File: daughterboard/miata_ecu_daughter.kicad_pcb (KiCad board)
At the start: 4 copper layers, 125 x 60 mm, 232 parts, among them J1 Mezz_Power_Out, J102 SWD (WBO), J2 Mezz_Signal_In, J3 SWD, Q1 AUIPS2041LTR, Q101 VND14NV04, Q2 AUIPS2041LTR, Q3 AUIPS2041LTR, Q4 AUIPS2041LTR, Q5 AUIPS2041LTR, Q6 AUIPS2041LTR, Q7 AUIPS2041LTR, Q8 AUIPS2041LTR, SW1 BOOT, SW2 RESET, U1 STM32F407VGT6, U10 SN65HVD230DR, U101 MCP6004, U102 STM32F042K6T6, U103 REF3033, U105 AD8628, U106 SN65HVD230DR, U11 SN74LVC4245APWR, U2 LMR14020, U3 TLS115B0EJ, U4 AMS1117-3.3, U5 ULN2003AD, U6 TC4427, U7 TC4427, U8 LMV321IDBVR, U9 MAX9926UAEE+, Y1 8MHz

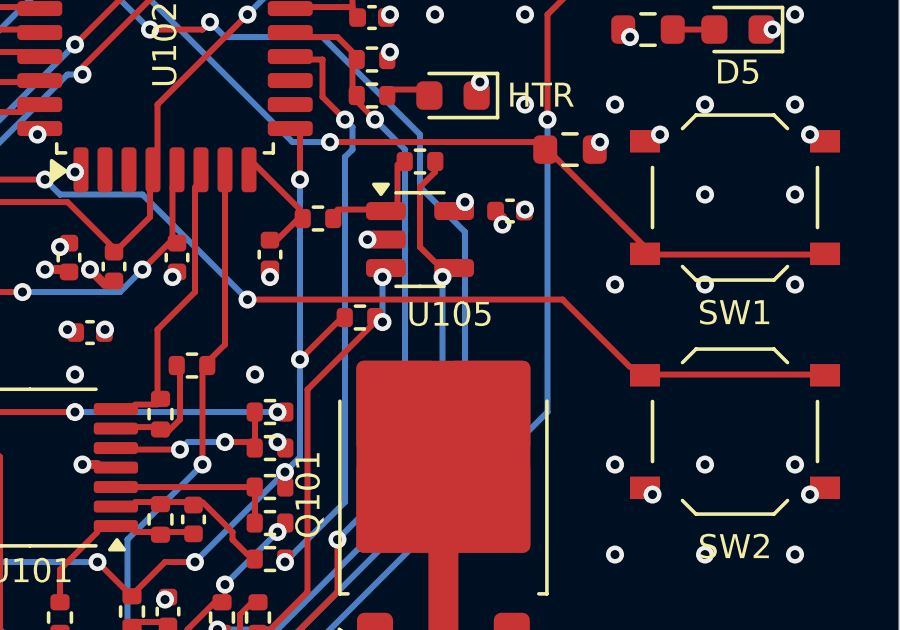
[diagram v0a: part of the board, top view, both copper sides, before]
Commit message: Daughterboard rev 0.5b: in-stock parts for JLCPCB assembly
JLCPCB's BOM check flagged ten lines short of stock and one footprint mismatch.
All replacements are in stock at JLCPCB and fit the existing footprints (no re-route):
- Q1-Q8: onsemi NCV8406ASTT3G (C459816) instead of AUIPS2041LTR: same SOT-223
  pinout, 60-70 V active clamp, current limit, thermal shutdown, AEC-Q101.
- D11/D12 Littelfuse SMAJ33A (C223988); F1 TECHFUSE nSMD050-33V (C70077);
  L1 FH CMI322513U2R2KT (C70960); LEDs KENTO KT-0603G/B/Y; C103 YAGEO 33 nF
  50 V (C106862); R110 62 ohm 1% (C23222, was 61.9).
- U9 (MAX9926, spare VR inputs, out of stock everywhere) not fitted.
- U105 footprint renamed SOT-23-5 (AD8628ARTZ; pads identical to TSOT-23-5).
- JLC BOM: one line per LCSC part (SW1/SW2); not-fitted parts excluded.

Re-checked: netlist 754 pads 0 differences, DRC 0 unconnected / 0 clearance,
circuit sims with the NCV8406A model 20 OK / 3 CHECK / 6 REF / 0 FAIL.

Co-Authored-By: Claude Opus 5.5 <noreply@anthropic.com>
Claude-Session: https://claude.ai/code/session_012UFcA8PhPqkqYxcgEjD2n9
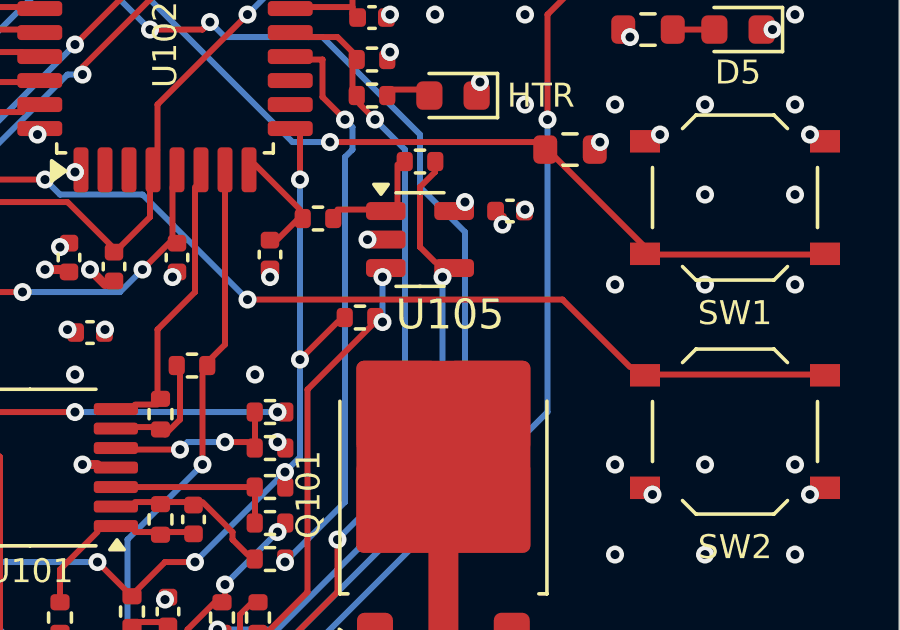
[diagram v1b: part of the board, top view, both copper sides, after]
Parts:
- F1: value SMD1206P050TF/24 -> nSMD050-33V
- Q1, Q2, Q3, Q4, Q5, Q6, Q7, Q8: value AUIPS2041LTR -> NCV8406ASTT3G
- R110: value 61.9 -> 62
- U105: footprint Package_TO_SOT_SMD:TSOT-23-5 -> Package_TO_SOT_SMD:SOT-23-5
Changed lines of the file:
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@@
         (effects (font (size 0.8 0.8) (thickness 0.12)))
     )
-    (fp_text value "AUIPS2041LTR" (at 0 4.5 90) (layer "F.Fab") hide
+    (fp_text value "NCV8406ASTT3G" (at 0 4.5 90) (layer "F.Fab") hide
         (effects (font (size 1 1) (thickness 0.15)))
     )
@@
     )
   )
+  (footprint "Package_TO_SOT_SMD:SOT-23-5" (layer "F.Cu")
+    (at 209 89)
+    (descr "SOT, 5 Pin (https://www.jedec.org/sites/default/files/docs/Mo-178c.PDF variant AA), generated with kicad-footprint-generator ipc_gullwing_generator.py")
+    (tags "SOT TO_SOT_SMD")
+    (attr smd)
+    (fp_text reference "U105" (at 1 2.5) (layer "F.SilkS")
+        (effects (font (size 1 1) (thickness 0.15)))
+    )
+    (fp_text value "AD8628" (at 0 2.4) (layer "F.Fab") hide
+        (effects (font (size 1 1) (thickness 0.15)))
+    )
+    (fp_text user "${REFERENCE}" (at 0 0) (layer "F.Fab")
+        (effects (font (size 0.4 0.4) (thickness 0.06)))
+    )
+    (fp_line (start 0 -1.56) (end -0.8 -1.56)
+      (stroke (width 0.12) (type solid)) (layer "F.SilkS"))
+    (fp_line (start 0 -1.56) (end 0.8 -1.56)
+      (stroke (width 0.12) (type solid)) (layer "F.SilkS"))
+    (fp_line (start 0 1.56) (end -0.8 1.56)
+      (stroke (width 0.12) (type solid)) (layer "F.SilkS"))
+    (fp_line (start 0 1.56) (end 0.8 1.56)
+      (stroke (width 0.12) (type solid)) (layer "F.SilkS"))
+    (fp_poly
+      (pts
+        (xy -1.3 -1.51)
+        (xy -1.54 -1.84)
+        (xy -1.06 -1.84)
+        (xy -1.3 -1.51)
+      )
+      (stroke (width 0.12) (type solid)) (fill solid) (layer "F.SilkS"))
+    (fp_line (start -2.05 -1.7) (end -2.05 1.7)
+      (stroke (width 0.05) (type solid)) (layer "F.CrtYd"))
+    (fp_line (start -2.05 1.7) (end 2.05 1.7)
+      (stroke (width 0.05) (type solid)) (layer "F.CrtYd"))
+    (fp_line (start 2.05 -1.7) (end -2.05 -1.7)
+      (stroke (width 0.05) (type solid)) (layer "F.CrtYd"))
+    (fp_line (start 2.05 1.7) (end 2.05 -1.7)
+      (stroke (width 0.05) (type solid)) (layer "F.CrtYd"))
+    (fp_line (start -0.8 -1.05) (end -0.4 -1.45)
+      (stroke (width 0.1) (type solid)) (layer "F.Fab"))
+    (fp_line (start -0.8 1.45) (end -0.8 -1.05)
+      (stroke (width 0.1) (type solid)) (layer "F.Fab"))
+    (fp_line (start -0.4 -1.45) (end 0.8 -1.45)
+      (stroke (width 0.1) (type solid)) (layer "F.Fab"))
+    (fp_line (start 0.8 -1.45) (end 0.8 1.45)
+      (stroke (width 0.1) (type solid)) (layer "F.Fab"))
+    (fp_line (start 0.8 1.45) (end -0.8 1.45)
+      (stroke (width 0.1) (type solid)) (layer "F.Fab"))
+    (pad "1" smd roundrect (at -1.1375 -0.95) (size 1.325 0.6) (layers "F.Cu" "F.Paste" "F.Mask") (roundrect_rratio 0.25)
+      (net 162 "/Wideband controller/WB_IS_OUT"))
+    (pad "2" smd roundrect (at -1.1375 0) (size 1.325 0.6) (layers "F.Cu" "F.Paste" "F.Mask") (roundrect_rratio 0.25)
+      (net 39 "GND"))
+    (pad "3" smd roundrect (at -1.1375 0.95) (size 1.325 0.6) (layers "F.Cu" "F.Paste" "F.Mask") (roundrect_rratio 0.25)
+      (net 163 "/Wideband controller/WB_IS_P"))
+    (pad "4" smd roundrect (at 1.1375 0.95) (size 1.325 0.6) (layers "F.Cu" "F.Paste" "F.Mask") (roundrect_rratio 0.25)
+      (net 161 "/Wideband controller/WB_IS_N"))
+    (pad "5" smd roundrect (at 1.1375 -0.95) (size 1.325 0.6) (layers "F.Cu" "F.Paste" "F.Mask") (roundrect_rratio 0.25)
+      (net 4 "+3V3"))
+    (model "${KICAD7_3DMODEL_DIR}/Package_TO_SOT_SMD.3dshapes/SOT-23-5.wrl"
+      (offset (xyz 0 0 0))
+      (scale (xyz 1 1 1))
+      (rotate (xyz 0 0 0))
+    )
+  )
   (footprint "Resistor_SMD:R_0603_1608Metric" (layer "F.Cu")
     (at 115.6 92.6)
@@
         (effects (font (size 0.8 0.8) (thickness 0.12)))
     )
-    (fp_text value "AUIPS2041LTR" (at 0 4.5 90) (layer "F.Fab") hide
+    (fp_text value "NCV8406ASTT3G" (at 0 4.5 90) (layer "F.Fab") hide
         (effects (font (size 1 1) (thickness 0.15)))
     )
@@
         (effects (font (size 0.8 0.8) (thickness 0.12)))
     )
-    (fp_text value "61.9" (at 0 1.43) (layer "F.Fab") hide
+    (fp_text value "62" (at 0 1.43) (layer "F.Fab") hide
         (effects (font (size 1 1) (thickness 0.15)))
     )
@@
         (effects (font (size 0.8 0.8) (thickness 0.12)))
     )
-    (fp_text value "AUIPS2041LTR" (at 0 4.5 90) (layer "F.Fab") hide
+    (fp_text value "NCV8406ASTT3G" (at 0 4.5 90) (layer "F.Fab") hide
         (effects (font (size 1 1) (thickness 0.15)))
     )
@@
         (effects (font (size 0.8 0.8) (thickness 0.12)))
     )
-    (fp_text value "AUIPS2041LTR" (at 0 4.5 90) (layer "F.Fab") hide
+    (fp_text value "NCV8406ASTT3G" (at 0 4.5 90) (layer "F.Fab") hide
         (effects (font (size 1 1) (thickness 0.15)))
     )
@@
         (effects (font (size 0.8 0.8) (thickness 0.12)))
     )
-    (fp_text value "AUIPS2041LTR" (at 0 4.5 90) (layer "F.Fab") hide
+    (fp_text value "NCV8406ASTT3G" (at 0 4.5 90) (layer "F.Fab") hide
         (effects (font (size 1 1) (thickness 0.15)))
     )
@@
         (effects (font (size 0.8 0.8) (thickness 0.12)))
     )
-    (fp_text value "AUIPS2041LTR" (at 0 4.5 90) (layer "F.Fab") hide
+    (fp_text value "NCV8406ASTT3G" (at 0 4.5 90) (layer "F.Fab") hide
         (effects (font (size 1 1) (thickness 0.15)))
     )
@@
         (effects (font (size 0.8 0.8) (thickness 0.12)))
     )
-    (fp_text value "AUIPS2041LTR" (at 0 4.5 90) (layer "F.Fab") hide
+    (fp_text value "NCV8406ASTT3G" (at 0 4.5 90) (layer "F.Fab") hide
         (effects (font (size 1 1) (thickness 0.15)))
     )
@@
         (effects (font (size 0.8 0.8) (thickness 0.12)))
     )
-    (fp_text value "SMD1206P050TF/24" (at 0 1.82) (layer "F.Fab") hide
+    (fp_text value "nSMD050-33V" (at 0 1.82) (layer "F.Fab") hide
         (effects (font (size 1 1) (thickness 0.15)))
     )
@@
     )
   )
-  (footprint "Package_TO_SOT_SMD:TSOT-23-5" (layer "F.Cu")
-    (at 209 89)
-    (descr "TSOT, 5 Pin (https://www.jedec.org/sites/default/files/docs/MO-193D.pdf variant AB), generated with kicad-footprint-generator ipc_gullwing_generator.py")
-    (tags "TSOT TO_SOT_SMD")
-    (property "LCSC" "C29309")
-    (attr smd)
-    (fp_text reference "U105" (at 1 2.5) (layer "F.SilkS")
-        (effects (font (size 0.8 0.8) (thickness 0.12)))
-    )
-    (fp_text value "AD8628" (at 0 2.4) (layer "F.Fab") hide
-        (effects (font (size 1 1) (thickness 0.15)))
-    )
-    (fp_text user "${REFERENCE}" (at 0 0) (layer "F.Fab")
-        (effects (font (size 0.4 0.4) (thickness 0.06)))
-    )
-    (fp_line (start 0 -1.56) (end -0.8 -1.56)
-      (stroke (width 0.12) (type solid)) (layer "F.SilkS"))
-    (fp_line (start 0 -1.56) (end 0.8 -1.56)
-      (stroke (width 0.12) (type solid)) (layer "F.SilkS"))
-    (fp_line (start 0 1.56) (end -0.8 1.56)
-      (stroke (width 0.12) (type solid)) (layer "F.SilkS"))
-    (fp_line (start 0 1.56) (end 0.8 1.56)
-      (stroke (width 0.12) (type solid)) (layer "F.SilkS"))
-    (fp_poly
-      (pts
-        (xy -1.3 -1.51)
-        (xy -1.54 -1.84)
-        (xy -1.06 -1.84)
-        (xy -1.3 -1.51)
-      )
-      (stroke (width 0.12) (type solid)) (fill solid) (layer "F.SilkS"))
-    (fp_line (start -2.05 -1.7) (end -2.05 1.7)
-      (stroke (width 0.05) (type solid)) (layer "F.CrtYd"))
-    (fp_line (start -2.05 1.7) (end 2.05 1.7)
-      (stroke (width 0.05) (type solid)) (layer "F.CrtYd"))
-    (fp_line (start 2.05 -1.7) (end -2.05 -1.7)
-      (stroke (width 0.05) (type solid)) (layer "F.CrtYd"))
-    (fp_line (start 2.05 1.7) (end 2.05 -1.7)
-      (stroke (width 0.05) (type solid)) (layer "F.CrtYd"))
-    (fp_line (start -0.8 -1.05) (end -0.4 -1.45)
-      (stroke (width 0.1) (type solid)) (layer "F.Fab"))
-    (fp_line (start -0.8 1.45) (end -0.8 -1.05)
-      (stroke (width 0.1) (type solid)) (layer "F.Fab"))
-    (fp_line (start -0.4 -1.45) (end 0.8 -1.45)
-      (stroke (width 0.1) (type solid)) (layer "F.Fab"))
-    (fp_line (start 0.8 -1.45) (end 0.8 1.45)
-      (stroke (width 0.1) (type solid)) (layer "F.Fab"))
-    (fp_line (start 0.8 1.45) (end -0.8 1.45)
-      (stroke (width 0.1) (type solid)) (layer "F.Fab"))
-    (pad "1" smd roundrect (at -1.1375 -0.95) (size 1.325 0.6) (layers "F.Cu" "F.Paste" "F.Mask") (roundrect_rratio 0.25)
-      (net 162 "/Wideband controller/WB_IS_OUT"))
-    (pad "2" smd roundrect (at -1.1375 0) (size 1.325 0.6) (layers "F.Cu" "F.Paste" "F.Mask") (roundrect_rratio 0.25)
-      (net 39 "GND"))
-    (pad "3" smd roundrect (at -1.1375 0.95) (size 1.325 0.6) (layers "F.Cu" "F.Paste" "F.Mask") (roundrect_rratio 0.25)
-      (net 163 "/Wideband controller/WB_IS_P"))
-    (pad "4" smd roundrect (at 1.1375 0.95) (size 1.325 0.6) (layers "F.Cu" "F.Paste" "F.Mask") (roundrect_rratio 0.25)
-      (net 161 "/Wideband controller/WB_IS_N"))
-    (pad "5" smd roundrect (at 1.1375 -0.95) (size 1.325 0.6) (layers "F.Cu" "F.Paste" "F.Mask") (roundrect_rratio 0.25)
-      (net 4 "+3V3"))
-    (model "${KICAD7_3DMODEL_DIR}/Package_TO_SOT_SMD.3dshapes/TSOT-23-5.wrl"
-      (offset (xyz 0 0 0))
-      (scale (xyz 1 1 1))
-      (rotate (xyz 0 0 0))
-    )
-  )
   (footprint "Capacitor_SMD:C_0603_1608Metric" (layer "F.Cu")
     (at 153.2 72)
@@
         (effects (font (size 0.8 0.8) (thickness 0.12)))
     )
-    (fp_text value "AUIPS2041LTR" (at 0 4.5 90) (layer "F.Fab") hide
+    (fp_text value "NCV8406ASTT3G" (at 0 4.5 90) (layer "F.Fab") hide
         (effects (font (size 1 1) (thickness 0.15)))
     )

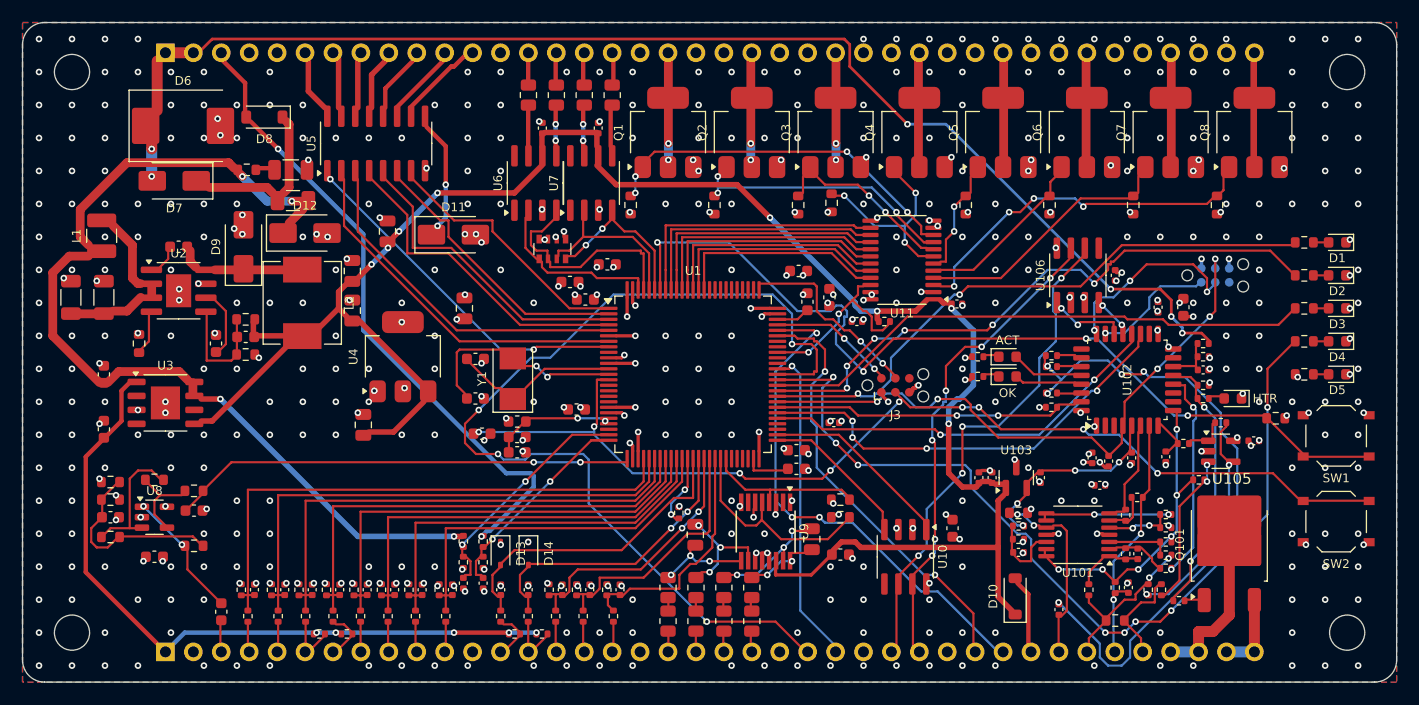
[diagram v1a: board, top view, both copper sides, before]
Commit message: Daughterboard rev 0.5b: LM2903 VR conditioner, JLC placement fix, parts-availability swaps
- U9: the out-of-stock, single-source MAX9926 is replaced by an LM2903 dual comparator (TI, onsemi, UMW, ST...).
  Each VR input gets a BAT54S clamp to GND/+5V and 100k to a 1.65 V bias, each output 1M of hysteresis
  (D15-D18, R73-R80, C60). Same output polarity, so J2 wiring and firmware are unchanged. circuit_sim.py
  section H covers it (25 OK / 4 CHECK / 6 REF / 0 FAIL).
- Re-routed; daughter_patch_05b.py (with hand_route.py) routes HALL1, which the autorouter left open, and
  moves AN_AUX3 clear of the new clamps. Netlist 778 pads, 0 differences; DRC 0 unconnected, 0 clearance.
- CPLs for all boards now use the gerbers' own coordinates, with JLC's per-package rotation offsets
  (SOT-223/TO-252/SOT-23 +180, SOIC/TSSOP/LQFP +270, resistor arrays +90).
- Parts-availability review swaps: motherboard F4 to TECHFUSE nSMD050-33V (C70077; the old PTC is out of
  stock), D6 to Littelfuse SMCJ30A, D9 to Diodes B360A. MPX5700AP (NRND), the harness headers and the
  STM32F042 are recorded as supply open items in VERIFICATION.md.
- Viewer assets and README renders rebuilt.

Co-Authored-By: Claude Opus 5.5 <noreply@anthropic.com>
Claude-Session: https://claude.ai/code/session_012UFcA8PhPqkqYxcgEjD2n9
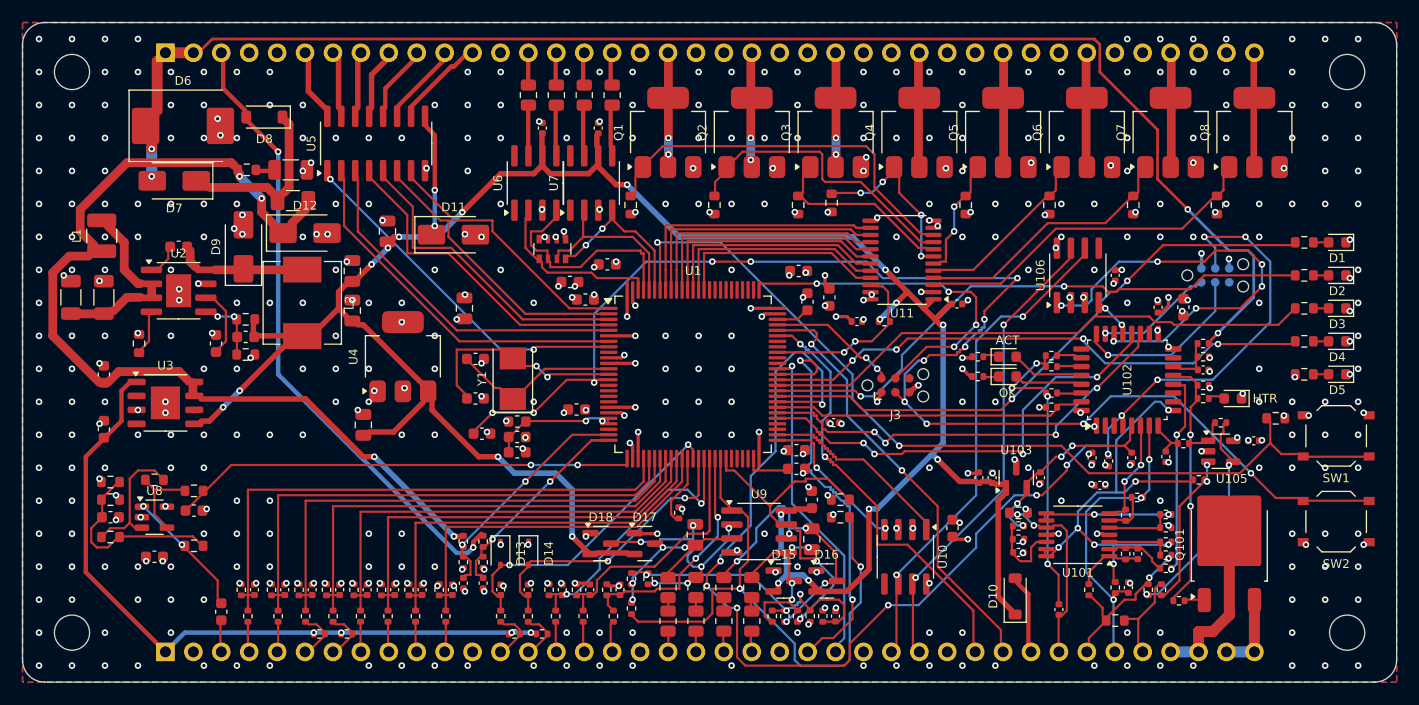
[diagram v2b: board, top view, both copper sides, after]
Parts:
- added C60: 100n, Capacitor_SMD:C_0402_1005Metric, F.Cu at (173.9, 104.0)
- added D15: BAT54S, Package_TO_SOT_SMD:SOT-23, F.Cu at (169.2, 100.8)
- added D16: BAT54S, Package_TO_SOT_SMD:SOT-23, F.Cu at (173.2, 100.8)
- added D17: BAT54S, Package_TO_SOT_SMD:SOT-23, F.Cu at (156.6, 97.4)
- added D18: BAT54S, Package_TO_SOT_SMD:SOT-23, F.Cu at (152.6, 97.4)
- added R73: 100k, Resistor_SMD:R_0402_1005Metric, F.Cu at (168.2, 104.0)
- added R74: 100k, Resistor_SMD:R_0402_1005Metric, F.Cu at (169.3, 104.0)
- added R75: 100k, Resistor_SMD:R_0402_1005Metric, F.Cu at (155.4, 100.6)
- added R76: 100k, Resistor_SMD:R_0402_1005Metric, F.Cu at (156.9, 100.6)
- added R77: 1M, Resistor_SMD:R_0402_1005Metric, F.Cu at (170.5, 104.0)
- added R78: 1M, Resistor_SMD:R_0402_1005Metric, F.Cu at (155.4, 103.3)
- added R79: 10k, Resistor_SMD:R_0402_1005Metric, F.Cu at (171.7, 104.0)
- added R80: 10k, Resistor_SMD:R_0402_1005Metric, F.Cu at (172.8, 104.0)
- D9: value SS36 -> B360A
- U9: value MAX9926UAEE+ -> LM2903DR; footprint Package_SO:QSOP-16_3.9x4.9mm_P0.635mm -> Package_SO:SOIC-8_3.9x4.9mm_P1.27mm
- moved C50 5.64 mm to (171.8, 93.4), turned to 90 degrees
- moved U9 0.60 mm to (167.0, 96.3), turned to 0 degrees
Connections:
- U9 pad 1: GND -> VR2_OUT
- U9 pad 2: (no net) -> /Inputs/VR2_INN
- U9 pad 3: GND -> /Inputs/VR2_INP
- U9 pad 4: VR1_OUT -> GND
- U9 pad 5: VR2_OUT -> /Inputs/VR1_INP
- U9 pad 6: GND -> /Inputs/VR1_INN
- U9 pad 7: (no net) -> VR1_OUT
- U9 pad 8: GND -> +5V
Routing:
- net WB_NRST: track 54.3 -> 123.9 mm, vias 5 -> 12
- net UART_TX: track 89.0 -> 37.2 mm, vias 4 -> 2
- net +5V: track 153.5 -> 192.2 mm, vias 8 -> 18
- net VR2_OUT: track 18.8 -> 52.4 mm, vias 0 -> 2
- net /Wideband controller/WB_CAN_TX: track 6.22 -> 39.3 mm, vias 2 -> 6
- net /MCU/NRST: track 95.4 -> 127.7 mm, vias 9 -> 13
- net /Wideband controller/WB_ESR: track 58.3 -> 26.7 mm, vias 5 -> 4
- net /MCU/LED_ERR: track 81.2 -> 50.1 mm, vias 8 -> 4
- net /Inputs/VR_BIAS: track 0.00 -> 26.2 mm, vias 0 -> 3
- net VR1_OUT: track 13.9 -> 30.0 mm, vias 0 -> 2
- net /MCU/SWCLK: track 17.8 -> 32.5 mm, vias 2 -> 4
- net /Inputs/VR1_INN: track 9.35 -> 23.2 mm, vias 3 -> 5
- net /Wideband controller/WB_VM: track 27.5 -> 40.7 mm, vias 6 -> 7
- net VBAT_IN: track 114.4 -> 126.4 mm, vias 6 -> 4
- net /Inputs/VR2_INN: track 9.29 -> 21.2 mm, vias 3 -> 6
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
